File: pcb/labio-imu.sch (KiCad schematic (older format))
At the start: 11 parts, among them SW501 DIP_SWITCH_X04, U501 LSM303, U502 BMP180

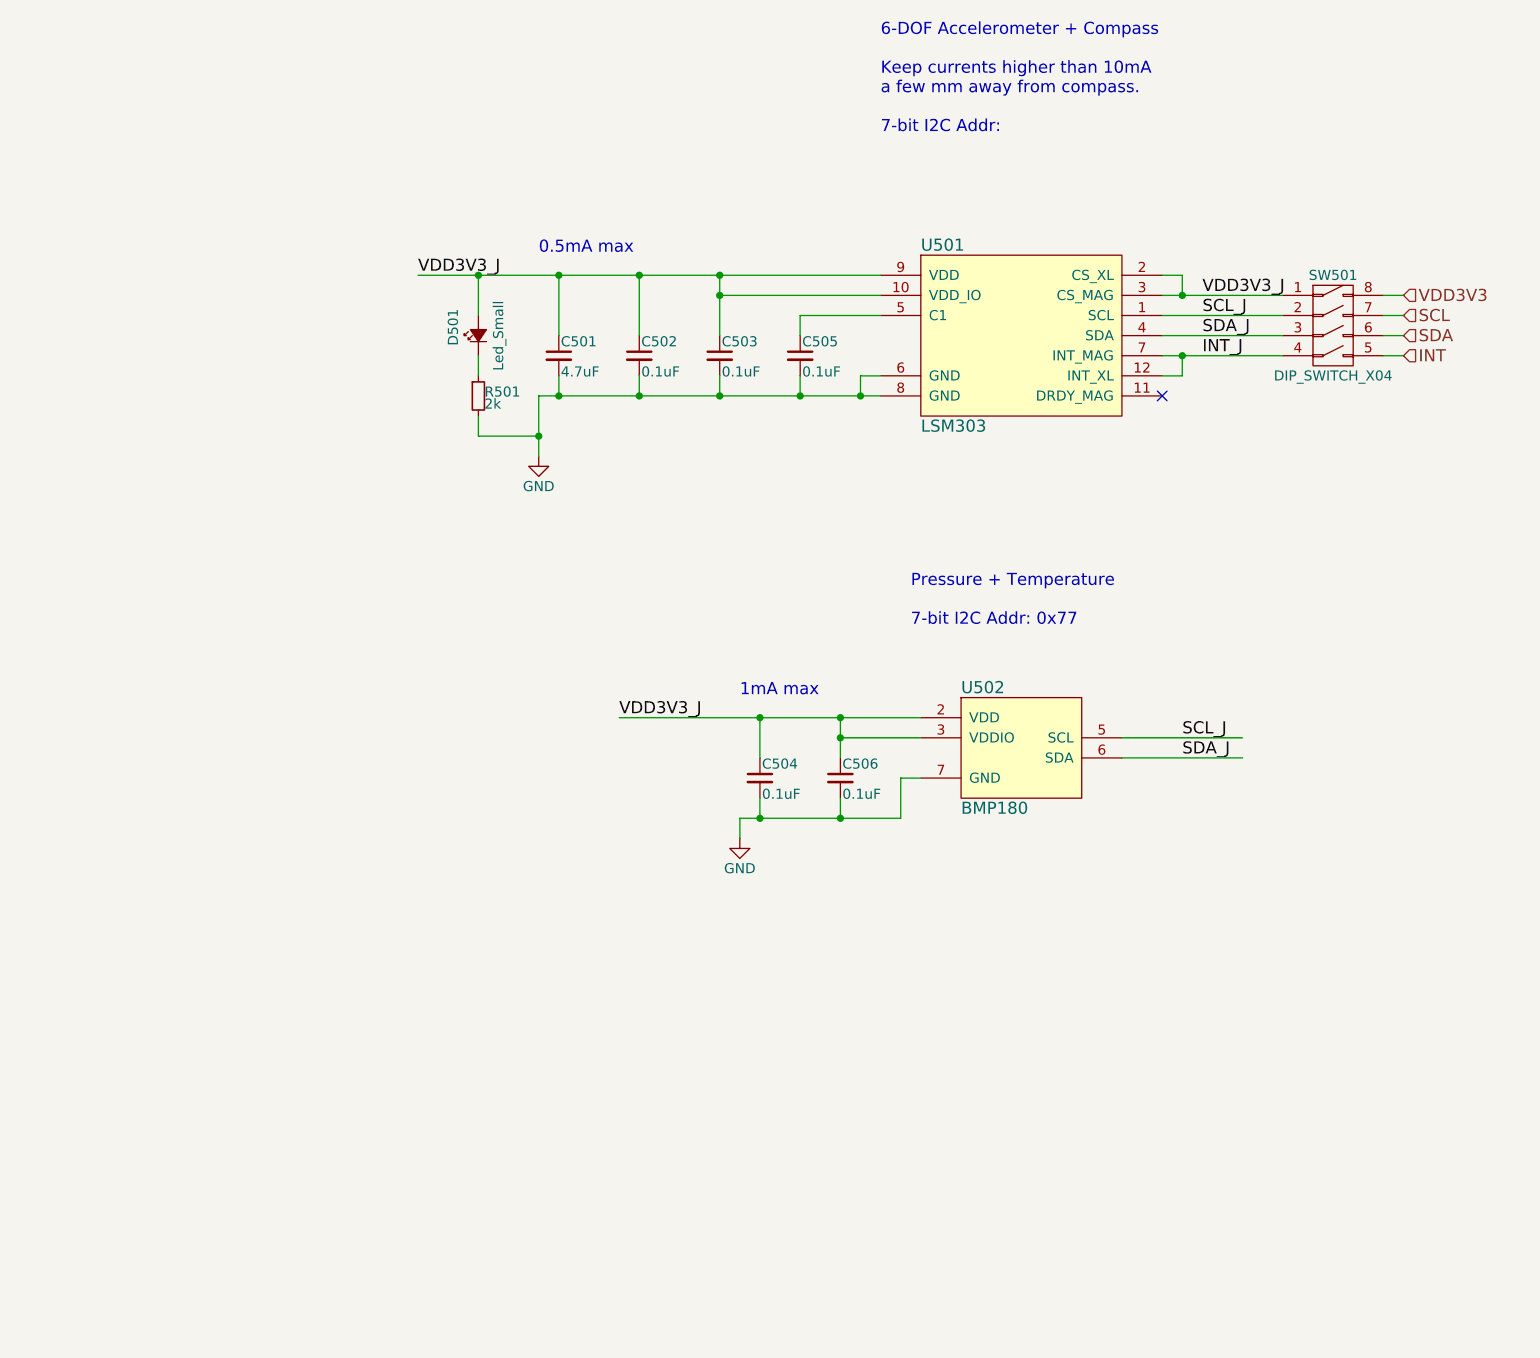
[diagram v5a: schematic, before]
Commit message: update imu parts, adc rails, motor headers
* replace LSM303C accelerometer with LSM303D for better sensor ranges at same cost.
* add L3GD20H gyroscope so we have a 10-DOF imu. consider leaving depopulated for complexity.
* add 0 ohms to accel/gyro address and interrupt pins in case of later changes
* change ADC rails to 5V to read 5V power shunts. add level shifters to the 3.3V I2C bus.
* use 3.5mm pitch headers for motor terminal blocks to accept higher guage wire.

todo:
* redo ADC routing
* make space behind motor headers
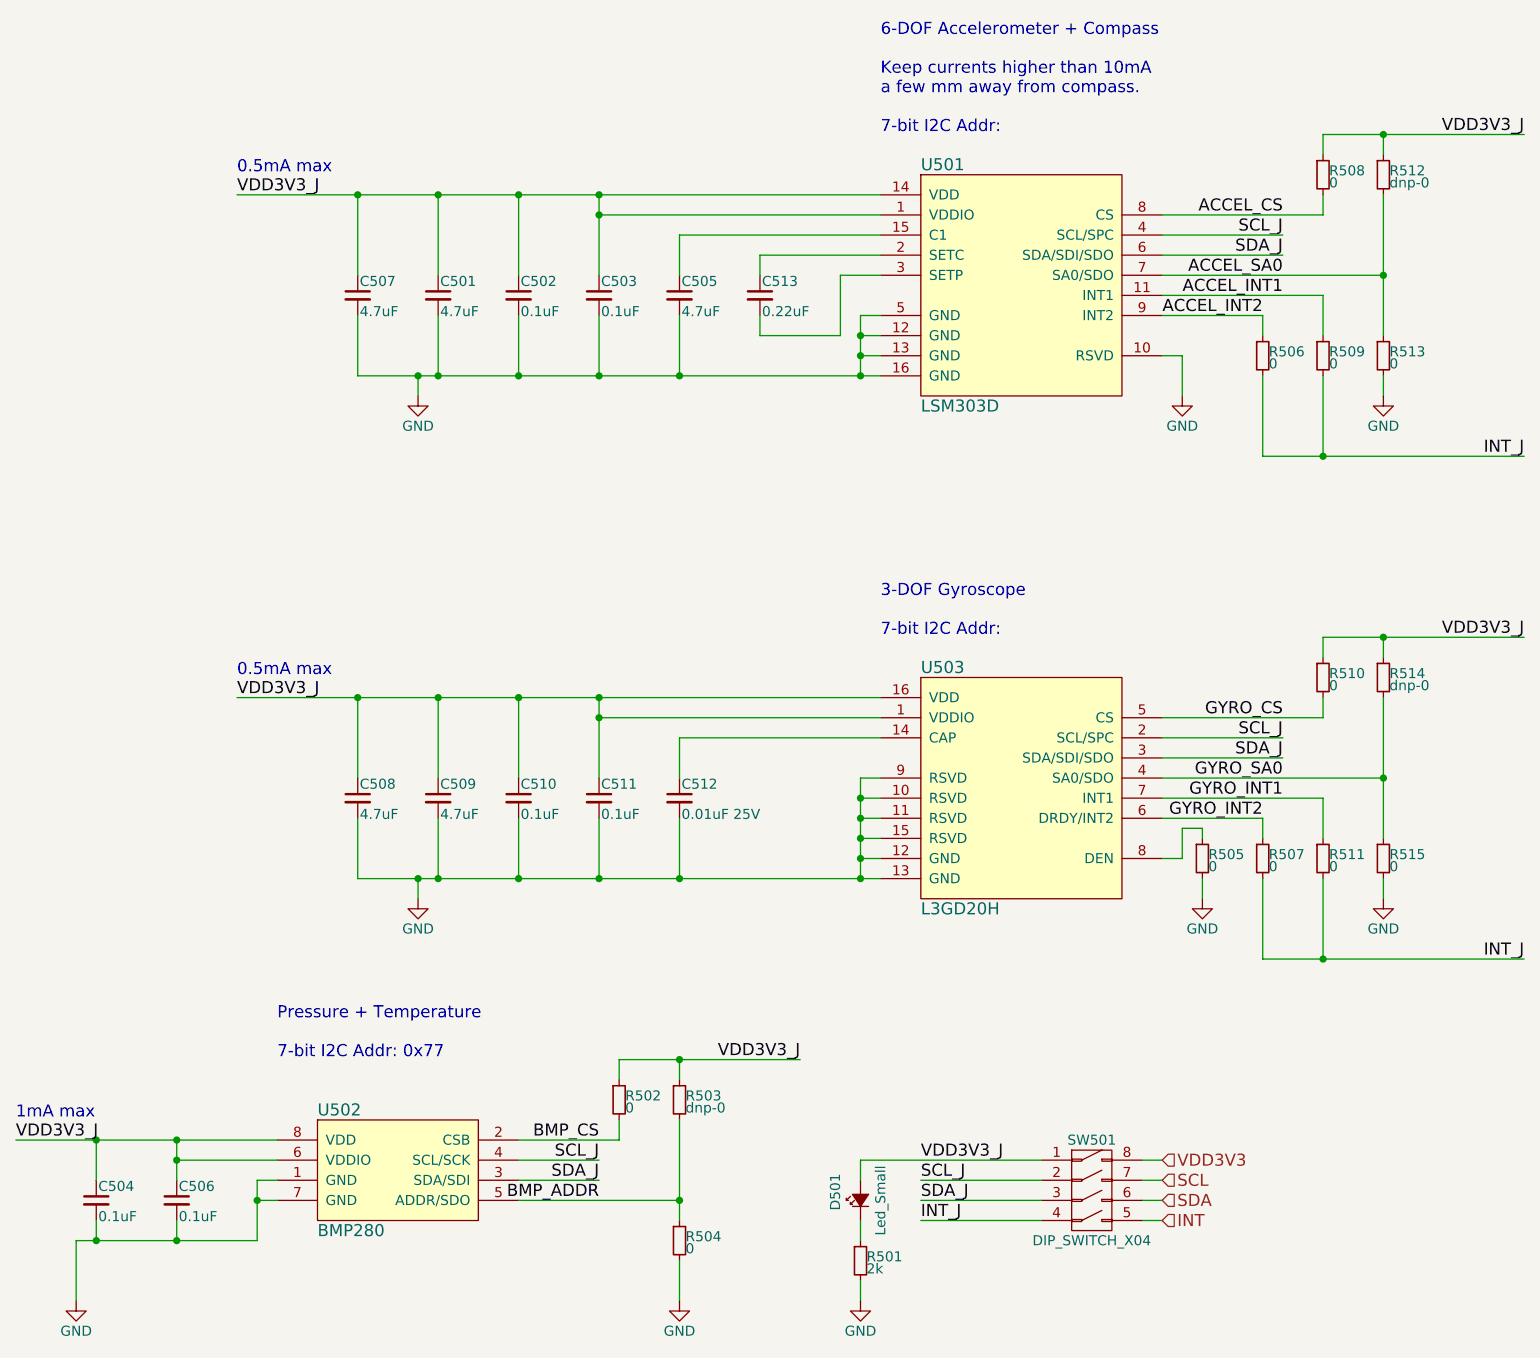
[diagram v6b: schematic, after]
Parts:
- removed U501: LSM303, labio-special:LSM303-LGA-12, symbol LSM303
- removed U502: BMP180, labio-special:BMP180-LGA-7, symbol BMP180
- added C507, C508, C509: 4.7uF, Capacitors_SMD:C_0805, symbol C_Small
- added C510, C511: 0.1uF, Capacitors_SMD:C_0603, symbol C_Small
- added C512: 0.01uF 25V, Capacitors_SMD:C_0603, symbol C_Small
- added C513: 0.22uF, Capacitors_SMD:C_0603, symbol C_Small
- added R502, R504, R505, R506, R507, R508, R509, R510, R511, R513, R515: 0, Resistors_SMD:R_0603, symbol R_Small
- added R503, R512, R514: dnp-0, Resistors_SMD:R_0603, symbol R_Small
- added U501: LSM303D, labio-special:LGA-16_3x3mm_Pitch0.5mm_ST, symbol LSM303D
- added U502: BMP280, labio-special:LGA-8_2.5x2.0mm_Pitch0.65mm_BMx280, symbol BMP280
- added U503: L3GD20H, labio-special:LGA-16_3x3mm_Pitch0.5mm_ST, symbol L3GD20H
- C505: value 0.1uF -> 4.7uF; footprint Capacitors_SMD:C_0603 -> Capacitors_SMD:C_0805
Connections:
- net labels added: ACCEL_CS, ACCEL_INT1, ACCEL_INT2, ACCEL_SA0, BMP_ADDR, BMP_CS, GYRO_CS, GYRO_INT1, GYRO_INT2, GYRO_SA0
- wire segments 43 -> 119
- no-connect marks 1 -> 0
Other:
- note added: "3-DOF Gyroscope\n\n7-bit I2C Addr:"
- moved on the sheet: C501, C502, C503, C504, C505, C506, D501, R501, SW501

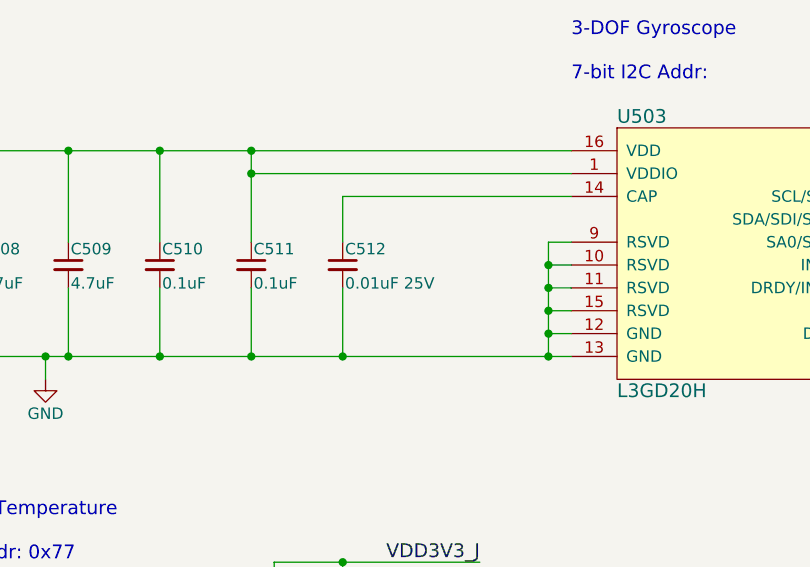
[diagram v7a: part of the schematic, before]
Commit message: add cmu + wise logos, clean up silk, review for final errors
* move audio jack in so copper pads are inside board
* add logos/identifier text on silk and copper
* change rpi connector for no paste (to be left depopulated at fab)
* change soldermask expansion to 2 mils/3 mils minimum width
* add labels for motor, ADC, codec headers
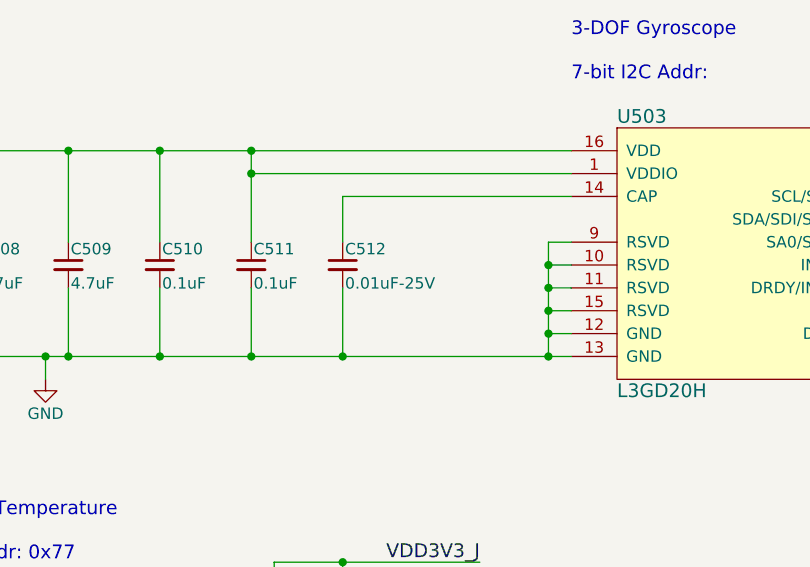
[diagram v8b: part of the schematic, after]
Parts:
- C512: value 0.01uF 25V -> 0.01uF-25V
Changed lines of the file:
@@
 LIBS:valves
 LIBS:labio-special
+LIBS:wise_logo
+LIBS:cmu_logo
 LIBS:labio-cache
 EELAYER 25 0
@@
 P 4100 4900
 F 0 "C512" H 4110 4970 50  0000 L CNN
-F 1 "0.01uF 25V" H 4110 4820 50  0000 L CNN
+F 1 "0.01uF-25V" H 4110 4820 50  0000 L CNN
 F 2 "Capacitors_SMD:C_0603" H 4100 4900 50  0001 C CNN
 F 3 "" H 4100 4900 50  0000 C CNN
